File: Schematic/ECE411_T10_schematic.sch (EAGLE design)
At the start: 23 parts, among them J1 1, J2 DCJ0202, Q1 1109200 Hz, U1 ATMEGA328P_PDIP, U2 LM386

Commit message: revisions
some quick revisions and cleanup after lecture 10/29
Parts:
- added HI_WRLD: 1, led:LEDSML1206
- added J3: AVR_SPI_PRG_6PTH, SparkFun-Connectors:AVR_SPI_PRG_6PTH
- added R5: 10k, resistor:R-US_M0805
- added R7: 333, resistor:R-US_M0805
- added S2: TAC_SWITCHSMD, SparkFun-Electromechanical:TAC_SWITCHSMD
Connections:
- new net N$10: R7.1, U1.PC0(ADC0)
- new net N$17: HI_WRLD.A, R7.2
- new net N$18: J3.3, U1.PB5(SCK)
- new net N$19: J3.1, U1.PB4(MISO)
- new net N$20: J3.4, U1.PB3(MOSI/OC2)
- new net RST: J3.5, R5.1, S2.3, S2.4, U1.PC6(/RESET)
- net GND: now also HI_WRLD.C, J3.6, S2.1, S2.2
- net SM1-CLK: now also SM1-3.1; no longer SM1-5.1
- net SM1-DAT: now also SM1-5.1; no longer SM1-3.1
- net VIN: now also J3.2, R5.2
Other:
- note added: "ISSUES: need Bill of Materials Rechargable battery cells and Power management circuit pending? Still reviewing LED strip constraints...LDP8806 not very well documented. TEST POINTSSS? block frames"
- note added: "This is the ISP programming header"
- note added: "This is the SM1 connector for the LED strip with LDP8806"
- note removed: "ISSUES: Something is weird with the labeling of V+/V- LM386, any ideas? need Bill of Materials Rechargable battery cells and Power management circuit pending? Still reviewing LED strip constraints...LDP8806 not very well documented."
- note removed: "This is the SM1 connector for the LED strip"
- moved on the sheet: C8, C9, D1, J1, J2, S1, SM1-1, SM1-3, SM1-5, SM1-6

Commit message: preliminary board layout
very preliminary
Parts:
- removed U2: LM386, SparkFun-AnalogIC:LM386
- added C10: 100nF, resistor:C-US025-024X044
- added IC1: LM386MM-1, linear:LM386MM-1
- added TP1, TP10, TP11, TP12, TP13, TP14, TP15, TP16, TP17, TP18, TP19, TP2, TP20, TP21, TP22, TP23, TP24, TP25, TP26, TP27, TP28, TP29, TP3, TP30, TP31, TP32, TP4, TP5, TP6, TP7, TP8, TP9: TPB1,27, testpad:TPB1,27
- C8: value 100pF -> 100nF
- C9: value 100pF -> 10uF
- Q1: value 1109200 Hz -> 8.192 MHz; device crystal:CRYSTALTC38H -> adafruit:CRYSTALHC49S
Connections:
- new net N$16: TP1.TP, U1.PD0(RXD)
- new net N$21: TP5.TP, U1.PD4(XCK/T0)
- new net N$22: TP2.TP, U1.PD1(TXD)
- new net N$23: TP3.TP, U1.PD2(INT0)
- new net N$24: TP4.TP, U1.PD3(INT1)
- new net N$25: TP6.TP, U1.PD5(T1)
- new net N$26: TP7.TP, U1.PD6(AIN0)
- new net N$27: TP8.TP, U1.PD7(AIN1)
- new net N$28: TP9.TP, U1.PC1(ADC1)
- new net N$29: TP10.TP, U1.PC2(ADC2)
- new net N$30: TP11.TP, U1.PC3(ADC3)
- new net N$31: C10.1, IC1.GND, TP21.TP
- net 3.3V: now also TP27.TP
- net GND: now also C10.2, IC1.+IN, IC1.BYPASS, TP24.TP; no longer U2.-IN, U2.BP, U2.V-
- net N$1: now also TP13.TP
- net N$11: now also TP23.TP
- net N$12: now also IC1.OUT, TP20.TP; no longer U2.OUT
- net N$15: now also TP29.TP
- net N$18: now also TP22.TP
- net N$19: now also TP12.TP
- net N$2: now also TP14.TP
- net N$20: now also TP25.TP
- net N$3: now also IC1.GAIN@1; no longer U2.GAIN@1
- net N$6: now also TP17.TP
- net N$7: now also IC1.GAIN@2; no longer U2.GAIN@8
- net N$8: now also IC1.-IN; no longer U2.+IN
- net RST: now also TP30.TP
- net SCL_5.0V: now also TP16.TP
- net SDA_5.0V: now also TP15.TP
- net SM1-CLK: now also TP19.TP
- net SM1-DAT: now also TP18.TP
- net VIN: now also IC1.VS, TP26.TP, TP28.TP, TP31.TP, TP32.TP; no longer U2.V+
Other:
- note added: "ISSUES: need Bill of Materials block frames"
- note removed: "ISSUES: need Bill of Materials Rechargable battery cells and Power management circuit pending? Still reviewing LED strip constraints...LDP8806 not very well documented. TEST POINTSSS? block frames"
- moved on the sheet: C3, C4, R1, R2

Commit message: layout preliminary final
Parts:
- removed SM1: 06FLZ-SM1, con-jst:06FLZ-SM1
- removed TP31, TP32: TPB1,27, testpad:TPB1,27
- added C11: 100nF, adafruit:C-US025-024X044
- added JP1: (no value), pinhead:PINHD-1X8
- added TP33, TP34, TP35, TP36: TPB1,27, testpad:TPB1,27
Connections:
- new net N$33: JP1.2, TP36.TP
- new net N$34: JP1.3, TP35.TP
- new net N$35: JP1.4, TP34.TP
- new net N$36: JP1.5, TP33.TP
- net GND: now also C11.2, JP1.8; no longer SM1-6.1
- net SM1-CLK: now also JP1.6; no longer SM1-3.1
- net SM1-DAT: now also JP1.7; no longer SM1-5.1
- net VIN: now also C11.1, JP1.1; no longer SM1-1.1, TP31.TP, TP32.TP
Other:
- note added: "This is the HDR connector for the LED strip with LDP8806"
- note removed: "This is the SM1 connector for the LED strip with LDP8806"
- moved on the sheet: TP18, TP19

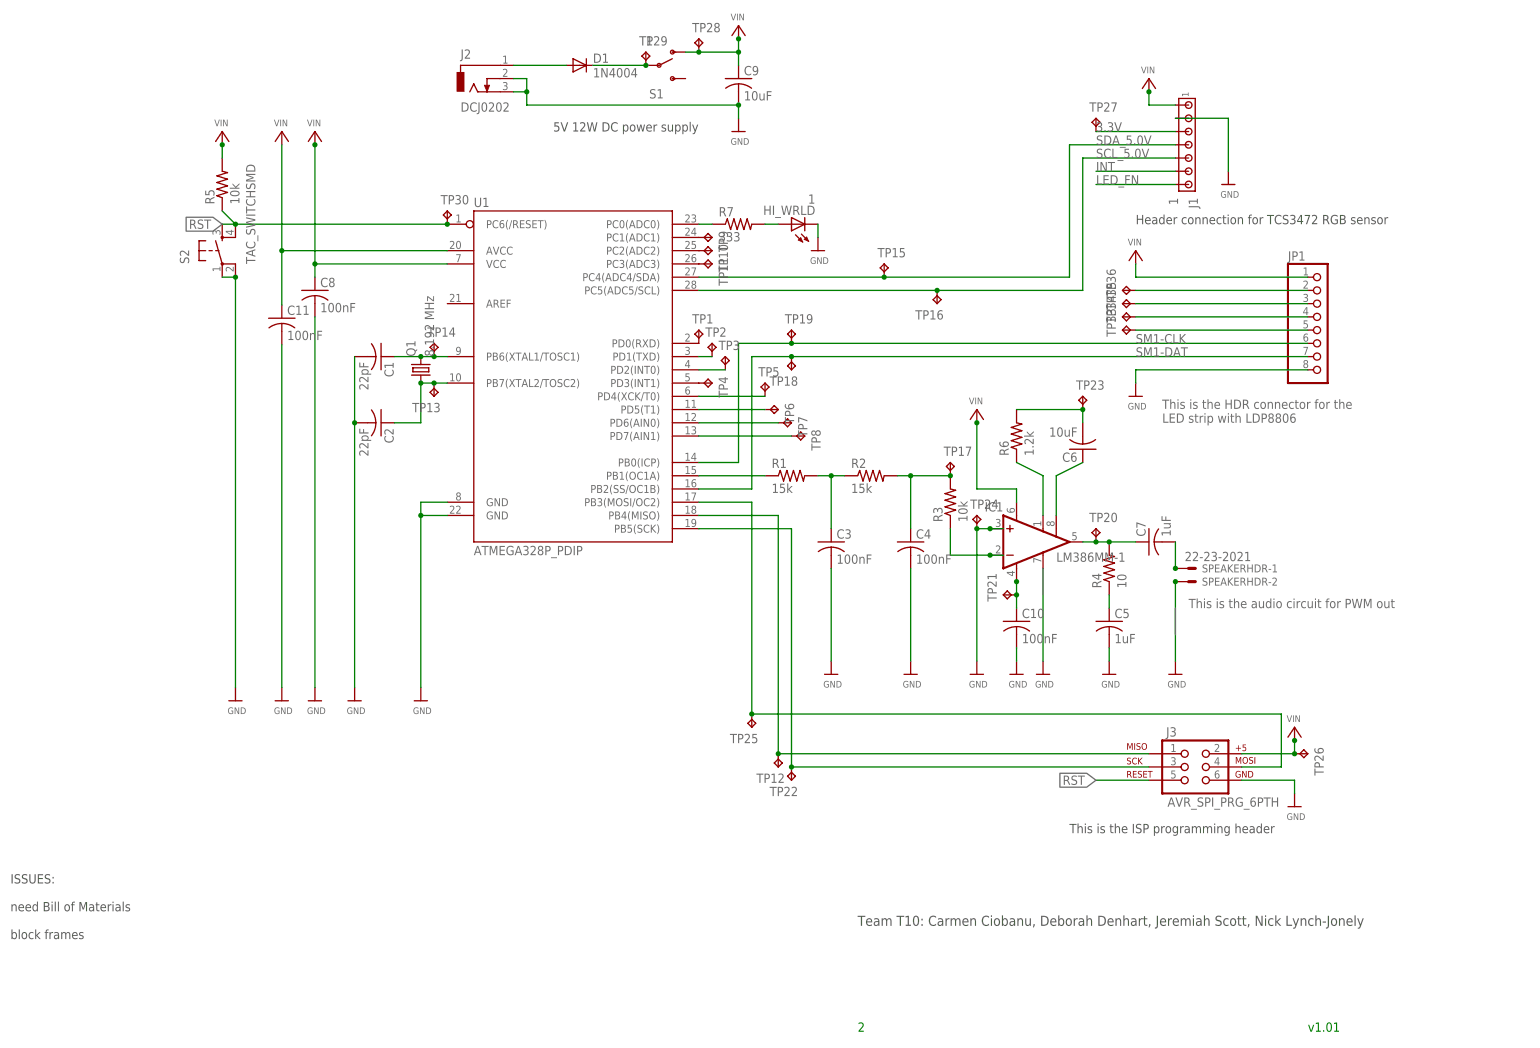
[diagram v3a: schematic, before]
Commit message: Preliminary board 2: electric boogaloo
completely rerouted the board with the correct size traces!
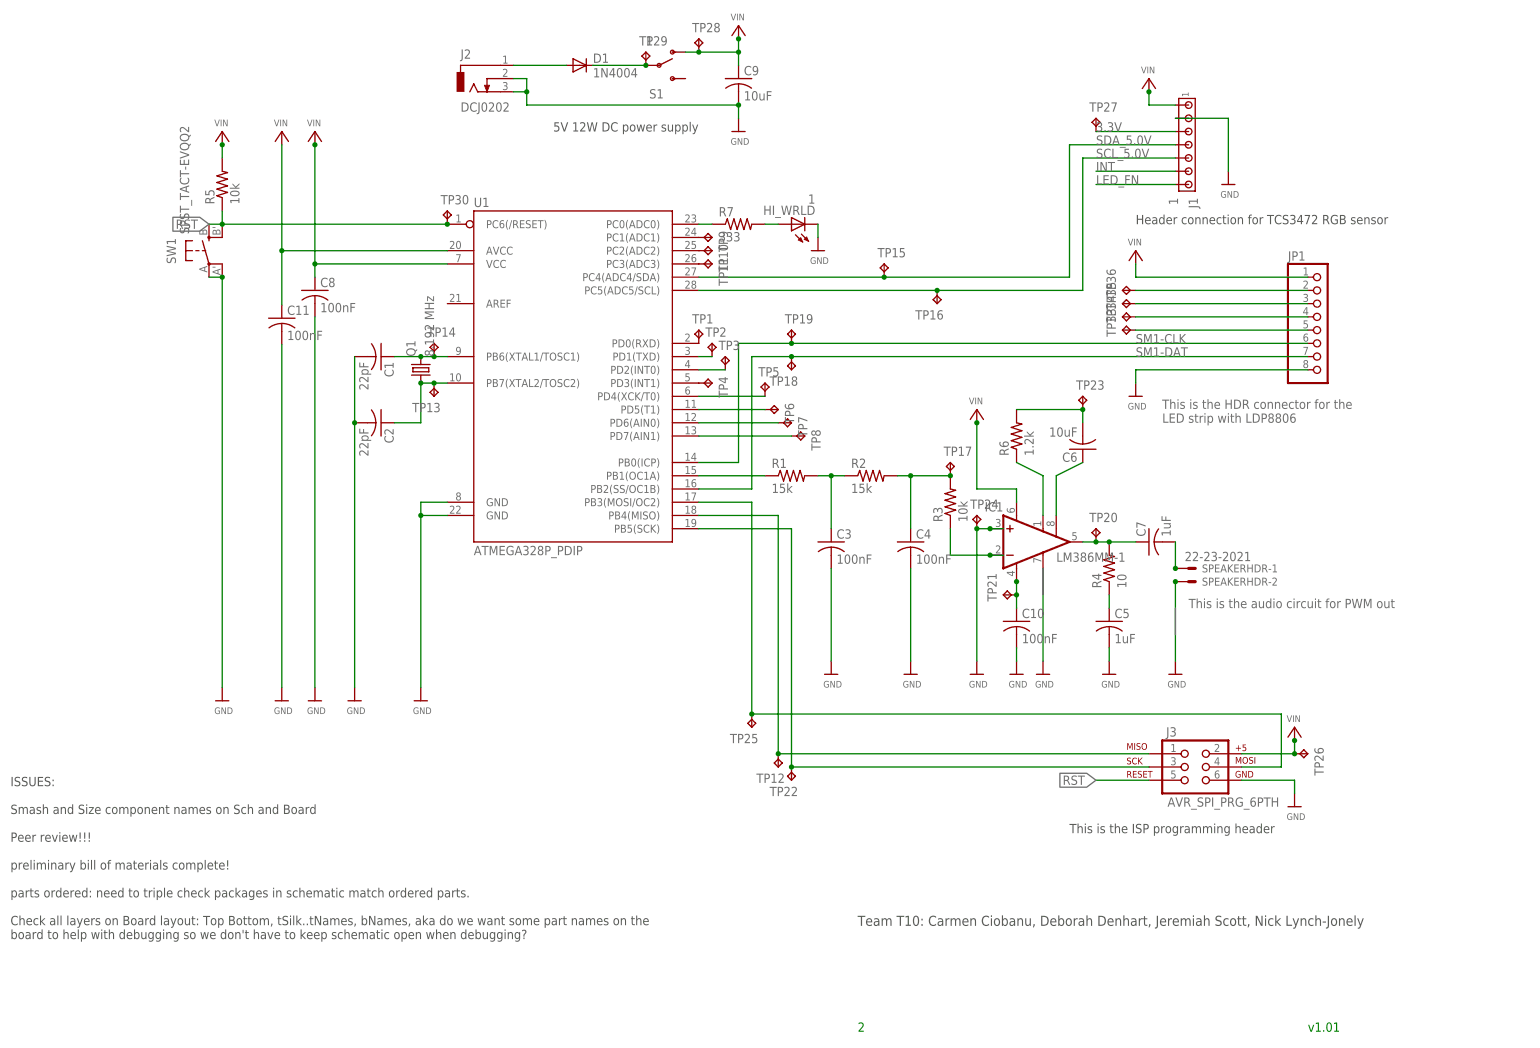
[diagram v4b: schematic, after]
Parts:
- removed S2: TAC_SWITCHSMD, SparkFun-Electromechanical:TAC_SWITCHSMD
- added SW1: SPST_TACT-EVQQ2, adafruit:SPST_TACT-EVQQ2
- C1, C10, C2, C3, C4, C5, C6, C7, C8, C9: device resistor:C-US025-024X044 -> resistor:C-USC0805
- C11: device adafruit:C-US025-024X044 -> adafruit:C-USC0805
- R1, R2: device resistor:R-US_R0402 -> resistor:R-US_M0805
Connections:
- net GND: now also SW1.P, SW1.P1; no longer S2.1, S2.2
- net RST: now also SW1.S, SW1.S1; no longer S2.3, S2.4
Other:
- note added: "ISSUES: Smash and Size component names on Sch and Board Peer review!!! preliminary bill of materials complete! parts ordered: need to triple check packages in schematic match ordered parts. Check all layers on Board layout: Top Bottom, tSilk..tNames, bNames, aka do we want some part names on the board to help with debugging so we don't have to keep schematic open when debugging?"
- note removed: "ISSUES: need Bill of Materials block frames"
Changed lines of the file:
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@@
 <setting verticaltext="up"/>
 </settings>
-<grid distance="0.01" unitdist="inch" unit="inch" style="lines" multiple="1" display="yes" altdistance="0.01" altunitdist="inch" altunit="inch"/>
+<grid distance="0.1" unitdist="inch" unit="inch" style="lines" multiple="1" display="no" altdistance="0.01" altunitdist="inch" altunit="inch"/>
 <layers>
 <layer number="1" name="Top" color="4" fill="1" visible="yes" active="no"/>
@@
 <part name="U1" library="SparkFun-DigitalIC" deviceset="ATMEGA328P_PDIP" device=""/>
 <part name="Q1" library="adafruit" deviceset="CRYSTAL" device="HC49S" value="8.192 MHz"/>
-<part name="C1" library="resistor" deviceset="C-US" device="025-024X044" value="22pF"/>
-<part name="C2" library="resistor" deviceset="C-US" device="025-024X044" value="22pF"/>
-<part name="R1" library="resistor" deviceset="R-US_" device="R0402" value="15k"/>
-<part name="R2" library="resistor" deviceset="R-US_" device="R0402" value="15k"/>
-<part name="C3" library="resistor" deviceset="C-US" device="025-024X044" value="100nF"/>
-<part name="C4" library="resistor" deviceset="C-US" device="025-024X044" value="100nF"/>
+<part name="C1" library="resistor" deviceset="C-US" device="C0805" value="22pF"/>
+<part name="C2" library="resistor" deviceset="C-US" device="C0805" value="22pF"/>
+<part name="R1" library="resistor" deviceset="R-US_" device="M0805" value="15k"/>
+<part name="R2" library="resistor" deviceset="R-US_" device="M0805" value="15k"/>
+<part name="C3" library="resistor" deviceset="C-US" device="C0805" value="100nF"/>
+<part name="C4" library="resistor" deviceset="C-US" device="C0805" value="100nF"/>
 <part name="R3" library="resistor" deviceset="R-US_" device="M0805" value="10k"/>
 <part name="R4" library="resistor" deviceset="R-US_" device="M0805" value="10"/>
-<part name="C5" library="resistor" deviceset="C-US" device="025-024X044" value="1uF"/>
-<part name="C6" library="resistor" deviceset="C-US" device="025-024X044" value="10uF"/>
-<part name="C7" library="resistor" deviceset="C-US" device="025-024X044" value="1uF"/>
+<part name="C5" library="resistor" deviceset="C-US" device="C0805" value="1uF"/>
+<part name="C6" library="resistor" deviceset="C-US" device="C0805" value="10uF"/>
+<part name="C7" library="resistor" deviceset="C-US" device="C0805" value="1uF"/>
 <part name="R6" library="resistor" deviceset="R-US_" device="M0805" value="1.2k"/>
 <part name="J1" library="con-amp" deviceset="MTA07-100" device="" value="1"/>
@@
 <part name="U$20" library="microbuilder" deviceset="GND" device=""/>
 <part name="U$21" library="microbuilder" deviceset="VIN" device=""/>
-<part name="C8" library="resistor" deviceset="C-US" device="025-024X044" value="100nF"/>
+<part name="C8" library="resistor" deviceset="C-US" device="C0805" value="100nF"/>
 <part name="U$8" library="microbuilder" deviceset="GND" device=""/>
 <part name="SPEAKERHDR" library="con-molex" deviceset="22-23-2021" device=""/>
@@
 <part name="D1" library="diode" deviceset="1N4004" device=""/>
 <part name="S1" library="SparkFun-Electromechanical" deviceset="SWITCH-SPDT" device="-SMD-A" value="1"/>
-<part name="C9" library="resistor" deviceset="C-US" device="025-024X044" value="10uF"/>
+<part name="C9" library="resistor" deviceset="C-US" device="C0805" value="10uF"/>
 <part name="U$1" library="microbuilder" deviceset="VIN" device=""/>
 <part name="U$6" library="microbuilder" deviceset="GND" device=""/>
@@
 <part name="U$5" library="microbuilder" deviceset="GND" device=""/>
 <part name="U$7" library="microbuilder" deviceset="VIN" device=""/>
-<part name="S2" library="SparkFun-Electromechanical" deviceset="TAC_SWITCH" device="SMD" value="TAC_SWITCHSMD"/>
 <part name="R5" library="resistor" deviceset="R-US_" device="M0805" value="10k"/>
 <part name="U$3" library="microbuilder" deviceset="GND" device=""/>
@@
 <part name="TP25" library="testpad" deviceset="TP" device="B1,27"/>
 <part name="TP26" library="testpad" deviceset="TP" device="B1,27"/>
-<part name="C10" library="resistor" deviceset="C-US" device="025-024X044" value="100nF"/>
+<part name="C10" library="resistor" deviceset="C-US" device="C0805" value="100nF"/>
 <part name="JP1" library="pinhead" deviceset="PINHD-1X8" device=""/>
 <part name="TP33" library="testpad" deviceset="TP" device="B1,27"/>
@@
 <part name="TP35" library="testpad" deviceset="TP" device="B1,27"/>
 <part name="TP36" library="testpad" deviceset="TP" device="B1,27"/>
-<part name="C11" library="adafruit" deviceset="C-US" device="025-024X044" value="100nF"/>
+<part name="C11" library="adafruit" deviceset="C-US" device="C0805" value="100nF"/>
 <part name="U$22" library="microbuilder" deviceset="GND" device=""/>
 <part name="5V3" library="microbuilder" deviceset="VIN" device=""/>
+<part name="SW1" library="adafruit" deviceset="SPST_TACT" device="-EVQQ2"/>
 </parts>
 <sheets>
@@
 <text x="30.48" y="-106.68" size="1.778" layer="91">2</text>
 <text x="-132.08" y="-88.9" size="1.778" layer="97">ISSUES:
-need Bill of Materials
-block frames</text>
+Smash and Size component names on Sch and Board
+Peer review!!!
+preliminary bill of materials complete!
+parts ordered: need to triple check packages in schematic match ordered parts.
+Check all layers on Board layout: Top Bottom, tSilk..tNames, bNames, aka do we want some part names on the
+board to help with debugging so we don't have to keep schematic open when debugging?
+</text>
 <text x="71.12" y="-68.58" size="1.778" layer="97">This is the ISP programming header</text>
 </plain>
@@
 <instance part="U$21" gate="G$1" x="83.82" y="40.64"/>
 <instance part="C8" gate="G$1" x="-73.66" y="35.56"/>
-<instance part="U$8" gate="G$1" x="-88.9" y="-43.18"/>
+<instance part="U$8" gate="G$1" x="-91.44" y="-43.18"/>
 <instance part="SPEAKERHDR" gate="-1" x="93.98" y="-17.78"/>
 <instance part="SPEAKERHDR" gate="-2" x="93.98" y="-20.32"/>
@@
 <instance part="U$5" gate="G$1" x="114.3" y="-63.5"/>
 <instance part="U$7" gate="G$1" x="114.3" y="-50.8"/>
-<instance part="S2" gate="S" x="-91.44" y="43.18" rot="R90"/>
 <instance part="R5" gate="G$1" x="-91.44" y="55.88" rot="R90"/>
 <instance part="U$3" gate="G$1" x="22.86" y="43.18"/>
@@
 <instance part="U$22" gate="G$1" x="-80.01" y="-43.18"/>
 <instance part="5V3" gate="G$1" x="-80.01" y="63.5"/>
+<instance part="SW1" gate="G$1" x="-93.98" y="43.18"/>
 </instances>
 <busses>
@@
 <segment>
 <pinref part="U$8" gate="G$1" pin="GND"/>
-<pinref part="S2" gate="S" pin="2"/>
-<pinref part="S2" gate="S" pin="1"/>
-<wire x1="-91.44" y1="38.1" x2="-88.9" y2="38.1" width="0.1524" layer="91"/>
-<wire x1="-88.9" y1="38.1" x2="-88.9" y2="-40.64" width="0.1524" layer="91"/>
-<junction x="-88.9" y="38.1"/>
+<wire x1="-93.98" y1="38.1" x2="-91.44" y2="38.1" width="0.1524" layer="91"/>
+<wire x1="-91.44" y1="38.1" x2="-91.44" y2="-40.64" width="0.1524" layer="91"/>
+<pinref part="SW1" gate="G$1" pin="P"/>
+<pinref part="SW1" gate="G$1" pin="P1"/>
+<junction x="-91.44" y="38.1"/>
 </segment>
 <segment>
@@
 <segment>
 <pinref part="U1" gate="G$1" pin="PC6(/RESET)"/>
-<pinref part="S2" gate="S" pin="4"/>
-<pinref part="S2" gate="S" pin="3"/>
-<wire x1="-88.9" y1="48.26" x2="-91.44" y2="48.26" width="0.1524" layer="91"/>
-<wire x1="-88.9" y1="48.26" x2="-91.44" y2="50.8" width="0.1524" layer="91"/>
+<wire x1="-91.44" y1="48.26" x2="-93.98" y2="48.26" width="0.1524" layer="91"/>
+<wire x1="-91.44" y1="48.26" x2="-91.44" y2="50.8" width="0.1524" layer="91"/>
 <pinref part="R5" gate="G$1" pin="1"/>
-<wire x1="-88.9" y1="48.26" x2="-48.26" y2="48.26" width="0.1524" layer="91"/>
+<wire x1="-91.44" y1="48.26" x2="-48.26" y2="48.26" width="0.1524" layer="91"/>
 <pinref part="TP30" gate="G$1" pin="TP"/>
-<junction x="-88.9" y="48.26"/>
+<junction x="-91.44" y="48.26"/>
 <junction x="-48.26" y="48.26"/>
-<label x="-91.44" y="48.26" size="1.778" layer="95" rot="R180" xref="yes"/>
-</segment>
-<segment>
+<label x="-93.98" y="48.26" size="1.778" layer="95" rot="R180" xref="yes"/>
+<pinref part="SW1" gate="G$1" pin="S"/>
+<pinref part="SW1" gate="G$1" pin="S1"/>
+</segment>
+<segment>
